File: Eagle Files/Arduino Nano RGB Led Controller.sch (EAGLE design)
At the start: 17 parts, among them J1 12V, M1 ARDUINO-NANO-3.0#ISP

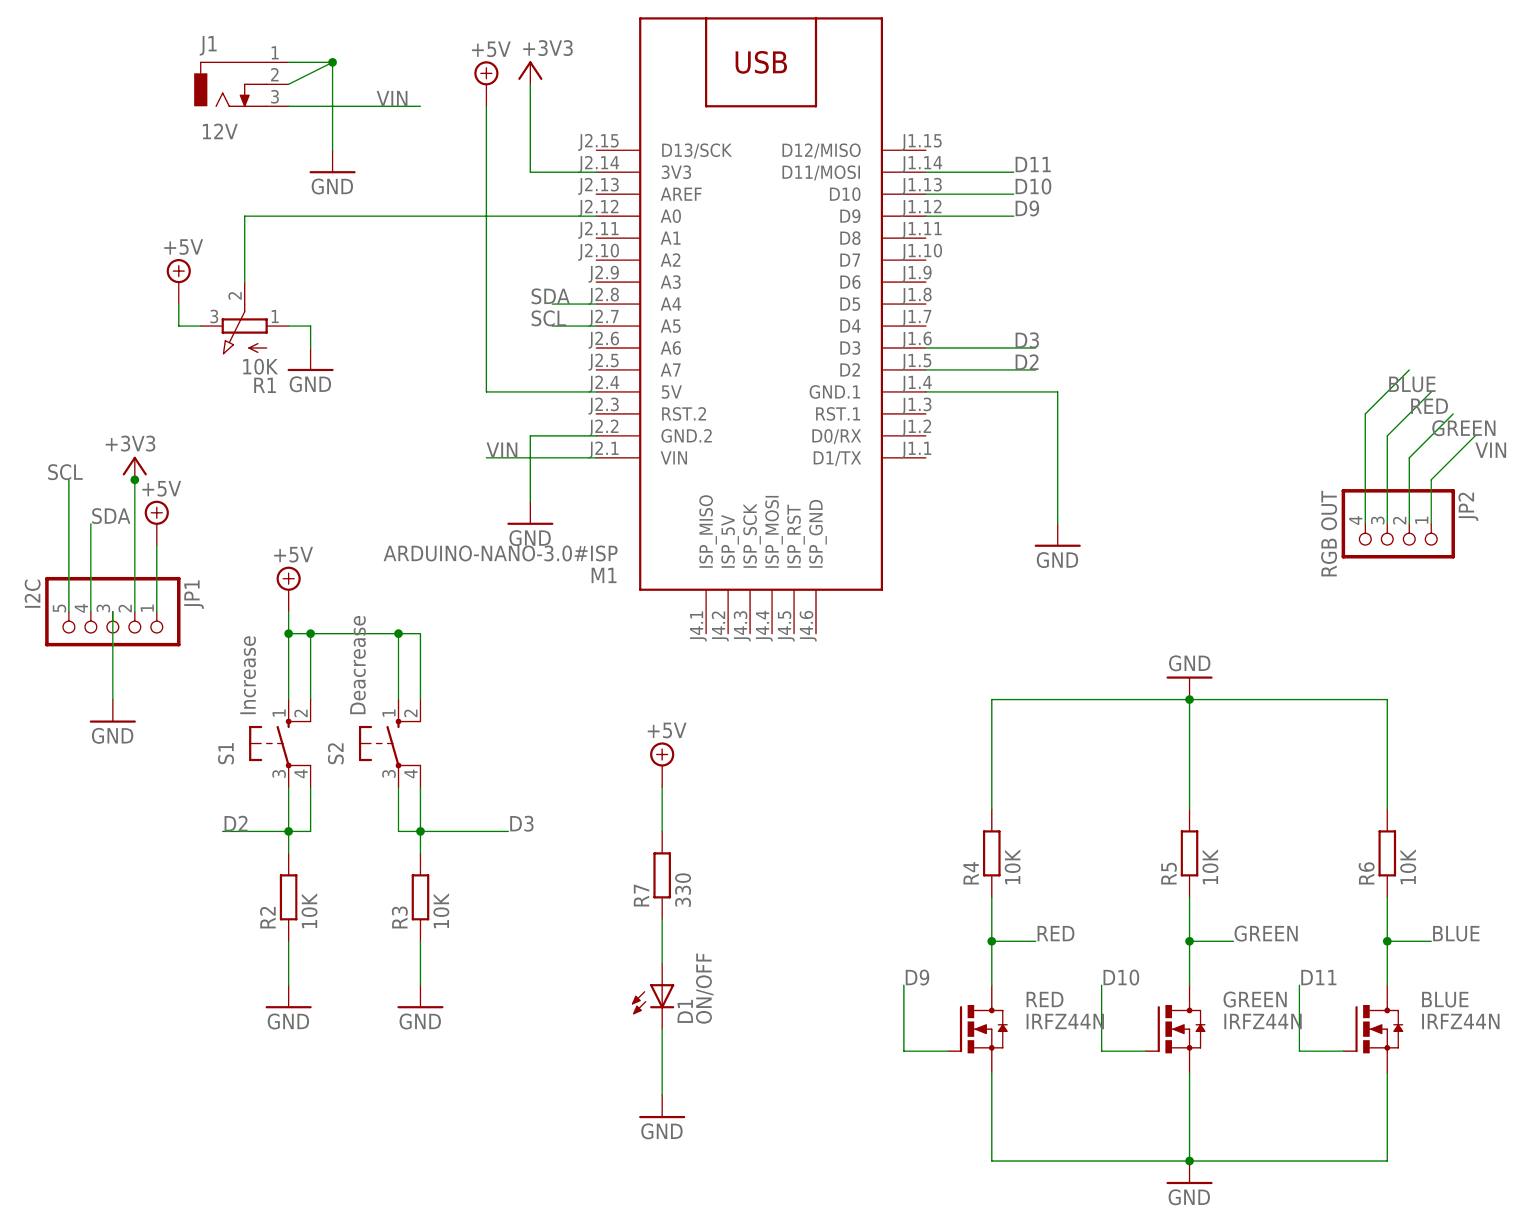
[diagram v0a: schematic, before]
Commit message: Logo added at pcb file
My Logo added at pcb file
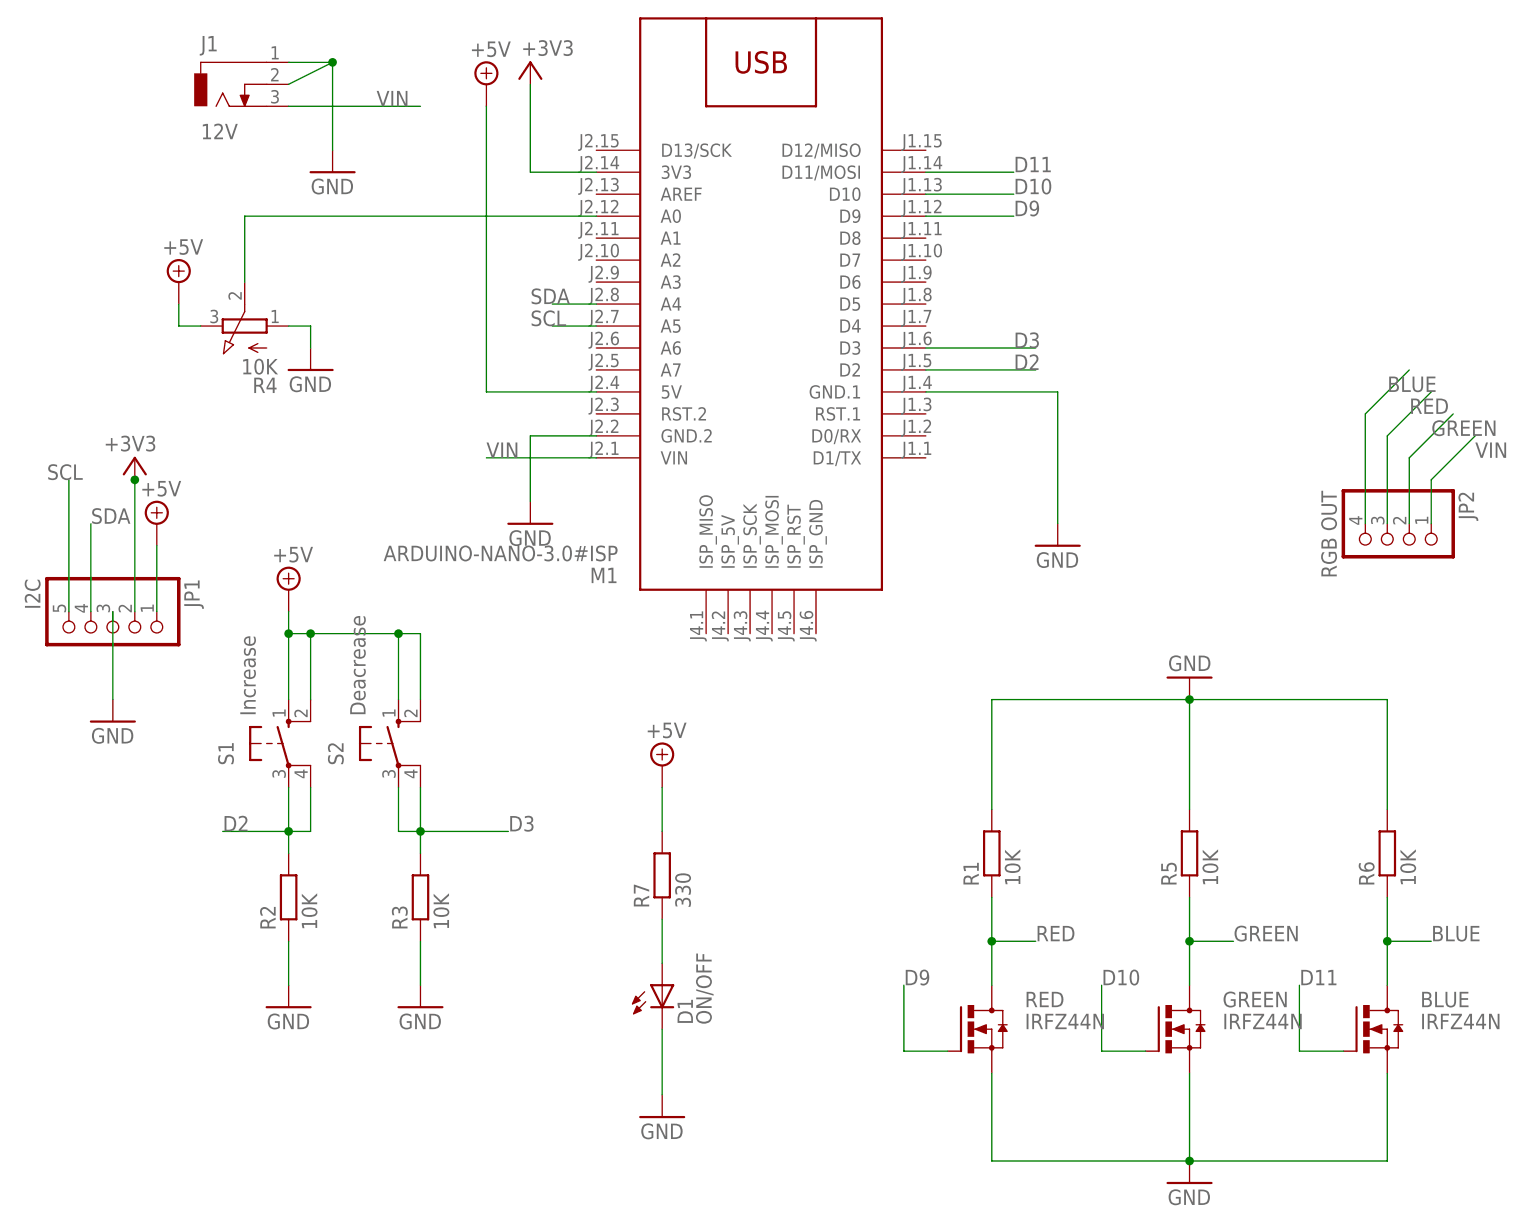
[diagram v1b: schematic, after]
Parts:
- R1: device pot:3RP/1610N -> rcl:R-EU_M1206
- R4: device rcl:R-EU_M1206 -> pot:3RP/1610N
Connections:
- net +5V: now also R4.E; no longer R1.E
- net GND: now also R1.2, R4.A; no longer R1.A, R4.2
- net N$1: now also R4.S; no longer R1.S
- net RED: now also R1.1; no longer R4.1
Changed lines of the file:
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@@
 <part name="U$3" library="MyLibrary" deviceset="GND" device=""/>
 <part name="SUPPLY1" library="supply2" deviceset="+5V" device=""/>
-<part name="R1" library="pot" deviceset="3RP/1610N" device="" value="10K"/>
+<part name="R4" library="pot" deviceset="3RP/1610N" device="" value="10K"/>
 <part name="SUPPLY2" library="supply2" deviceset="+5V" device=""/>
 <part name="U$4" library="MyLibrary" deviceset="GND" device=""/>
@@
 <part name="BLUE" library="MySemicontuctors" deviceset="IRFZ44N" device=""/>
 <part name="U$8" library="MyLibrary" deviceset="GND" device=""/>
-<part name="R4" library="rcl" deviceset="R-EU_" device="M1206" value="10K"/>
+<part name="R1" library="rcl" deviceset="R-EU_" device="M1206" value="10K"/>
 <part name="R5" library="rcl" deviceset="R-EU_" device="M1206" value="10K"/>
 <part name="R6" library="rcl" deviceset="R-EU_" device="M1206" value="10K"/>
@@
 <instance part="U$3" gate="G$1" x="109.22" y="22.86"/>
 <instance part="SUPPLY1" gate="+5V" x="43.18" y="73.66"/>
-<instance part="R1" gate="G$1" x="15.24" y="45.72" rot="R90"/>
+<instance part="R4" gate="G$1" x="15.24" y="45.72" rot="R90"/>
 <instance part="SUPPLY2" gate="+5V" x="7.62" y="50.8"/>
 <instance part="U$4" gate="G$1" x="22.86" y="43.18"/>
@@
 <instance part="BLUE" gate="G$1" x="147.32" y="-35.56"/>
 <instance part="U$8" gate="G$1" x="124.46" y="-50.8"/>
-<instance part="R4" gate="G$1" x="101.6" y="-15.24" rot="R90"/>
+<instance part="R1" gate="G$1" x="101.6" y="-15.24" rot="R90"/>
 <instance part="R5" gate="G$1" x="124.46" y="-15.24" rot="R90"/>
 <instance part="R6" gate="G$1" x="147.32" y="-15.24" rot="R90"/>
@@
 </segment>
 <segment>
-<pinref part="R1" gate="G$1" pin="A"/>
+<pinref part="R4" gate="G$1" pin="A"/>
 <pinref part="U$4" gate="G$1" pin="GND"/>
 <wire x1="20.32" y1="45.72" x2="22.86" y2="45.72" width="0.1524" layer="91"/>
@@
 </segment>
 <segment>
-<pinref part="R4" gate="G$1" pin="2"/>
+<pinref part="R1" gate="G$1" pin="2"/>
 <pinref part="U$9" gate="G$1" pin="GND"/>
 <wire x1="101.6" y1="-10.16" x2="101.6" y2="2.54" width="0.1524" layer="91"/>
@@
 </segment>
 <segment>
-<pinref part="R1" gate="G$1" pin="E"/>
+<pinref part="R4" gate="G$1" pin="E"/>
 <pinref part="SUPPLY2" gate="+5V" pin="+5V"/>
 <wire x1="10.16" y1="45.72" x2="7.62" y2="45.72" width="0.1524" layer="91"/>
@@
 <wire x1="55.88" y1="58.42" x2="15.24" y2="58.42" width="0.1524" layer="91"/>
 <wire x1="15.24" y1="58.42" x2="15.24" y2="50.8" width="0.1524" layer="91"/>
-<pinref part="R1" gate="G$1" pin="S"/>
+<pinref part="R4" gate="G$1" pin="S"/>
 </segment>
 </net>
@@
 <net name="RED" class="1">
 <segment>
-<pinref part="R4" gate="G$1" pin="1"/>
+<pinref part="R1" gate="G$1" pin="1"/>
 <pinref part="RED" gate="G$1" pin="D"/>
 <wire x1="101.6" y1="-20.32" x2="101.6" y2="-25.4" width="0.1524" layer="91"/>

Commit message: update
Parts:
- removed J1: 12V, con-jack:DCJ0303
- added D2: 1N4004, diode:1N4004
- added J2: V-IN 12V 1.5A MAX, con-jack:JACK-PLUG1
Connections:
- new net N$3: D2.A, J2.3
- net GND: now also J2.1, J2.2; no longer J1.1, J1.2
- net VIN: now also D2.C; no longer J1.3
